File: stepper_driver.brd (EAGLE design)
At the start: 100 x 80 mm, 12 parts, among them IC1 L293D, IC2 L293D, Q1 IRLML5203, Q2 IRLML5203

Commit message: First draft artwork done
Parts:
- added U$6, U$7, U$8, U$9: (no value), holes:3,0
- moved JP3 67.5 mm to (3.81, 34.3), turned to 90 degrees
- moved JP4 28.5 mm to (38.1, 26.7)
- moved IC1 19.3 mm to (20.3, 38.1)
- moved IC2 19.3 mm to (20.3, 15.2)
- moved JP1 19.3 mm to (38.1, 38.1)
- moved JP6 19.3 mm to (38.1, 15.2)
- moved JP5 18.5 mm to (3.81, 26.7)
- moved JP2 13.5 mm to (3.81, 19.1)
- moved Q1 11.7 mm to (10.2, 24.1), turned to 0 degrees
- moved R1 9.16 mm to (21.6, 52.1), turned to 0 degrees
- moved Q2 6.84 mm to (10.2, 47.0), turned to 0 degrees
- moved R2 5.68 mm to (21.6, 49.5), turned to 0 degrees
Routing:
- net N$5: track 0.00 -> 63.9 mm, vias 0 -> 2
- net N$7: track 0.00 -> 49.5 mm
- net IC1_EN: track 0.00 -> 45.1 mm, vias 0 -> 2
- net S2: track 0.00 -> 41.1 mm, vias 0 -> 2
- net S1: track 0.00 -> 35.2 mm, vias 0 -> 2
- net 5V: track 0.00 -> 34.6 mm
- net IC2_EN: track 0.00 -> 34.2 mm
- net VCC: track 0.00 -> 31.4 mm
- net N$3: track 15.8 -> 18.6 mm, vias 0 -> 1
- net N$8: track 15.8 -> 18.6 mm, vias 0 -> 1
- net N$9: track 15.8 -> 18.6 mm, vias 0 -> 1
- net N$2: track 15.8 -> 18.6 mm, vias 0 -> 1
- net N$6: track 29.2 -> 27.3 mm, vias 2 -> 1
- net N$11: track 29.2 -> 27.3 mm, vias 2 -> 1
- net N$4: track 29.2 -> 27.3 mm, vias 2 -> 1
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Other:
- board size 100 x 80 mm -> 42.9 x 55.9 mm
- board text added: "2012 Homin Lee"
- board text added: "Dual L293D driver"

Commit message: Polishing artwork
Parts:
- added C1, C2: (no value), rcl:C1206
- added LED1: (no value), led:LED5MM
- added R3, R4, R5: 1k, rcl:0207/10
- R1, R2: value (none) -> 10k
- moved R1 24.3 mm to (24.1, 27.9)
- moved U$7 4.02 mm to (35.6, 53.3)
- moved U$9 3.81 mm to (35.6, 3.81)
- moved Q2 1.80 mm to (11.4, 45.7)
- moved JP1 1.27 mm to (36.8, 38.1)
- moved JP4 1.27 mm to (36.8, 26.7)
- moved JP6 1.27 mm to (36.8, 15.2)
- moved U$8 1.27 mm to (3.81, 53.3)
- moved JP2 1.27 mm to (2.54, 19.1)
- moved JP3 1.27 mm to (2.54, 34.3)
- moved JP5 1.27 mm to (2.54, 26.7)
- moved IC1 1.27 mm to (19.1, 38.1)
- moved IC2 1.27 mm to (19.1, 15.2)
- moved R2 1.27 mm to (21.6, 50.8), turned to 180 degrees
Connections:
- new net N$10: LED1.K, R3.2
- new net N$12: Q1.3, R1.2, R5.2
- new net N$13: Q2.3, R2.2, R4.1
- net 5V: now also C1.1, C2.1, LED1.A
- net GND: now also C1.2, C2.2, R3.1
- net N$5: now also R5.1; no longer Q1.3, R1.2
- net N$7: now also R4.2; no longer Q2.3, R2.2
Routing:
- net N$5: track 63.9 -> 28.6 mm, vias 2 -> 0
- net N$12: track 0.00 -> 24.0 mm, vias 0 -> 2
- net N$7: track 49.5 -> 30.8 mm
- net N$10: track 0.00 -> 11.0 mm
- net 5V: track 34.6 -> 43.8 mm
- net N$13: track 0.00 -> 8.26 mm
- net IC2_EN: track 34.2 -> 37.9 mm, vias 0 -> 2
- net S2: track 41.1 -> 38.8 mm
- net N$6: track 27.3 -> 26.2 mm
- net N$4: track 27.3 -> 26.2 mm
- net N$11: track 27.3 -> 26.2 mm
- net N$1: track 27.3 -> 26.2 mm
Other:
- board size 42.9 x 55.9 mm -> 39 x 57.1 mm

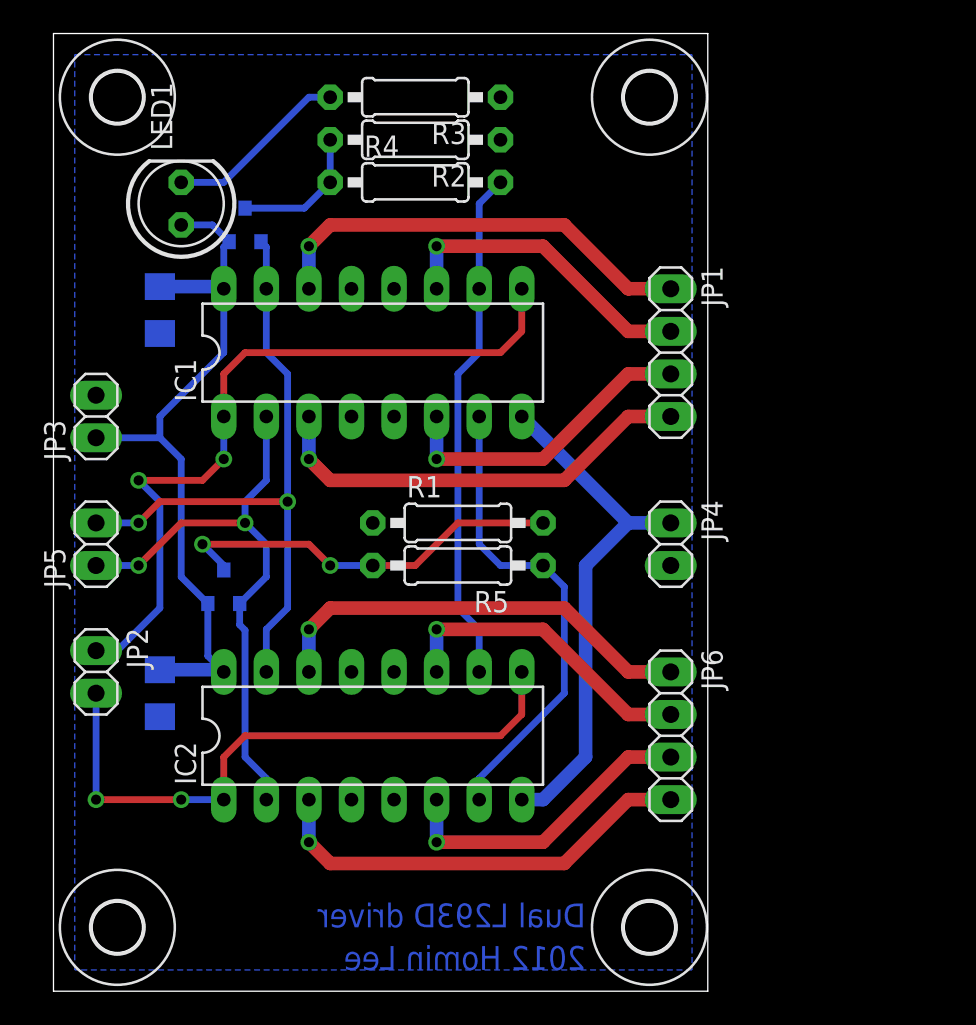
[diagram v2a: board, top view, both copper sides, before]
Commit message: Fix to only for single L293D IC
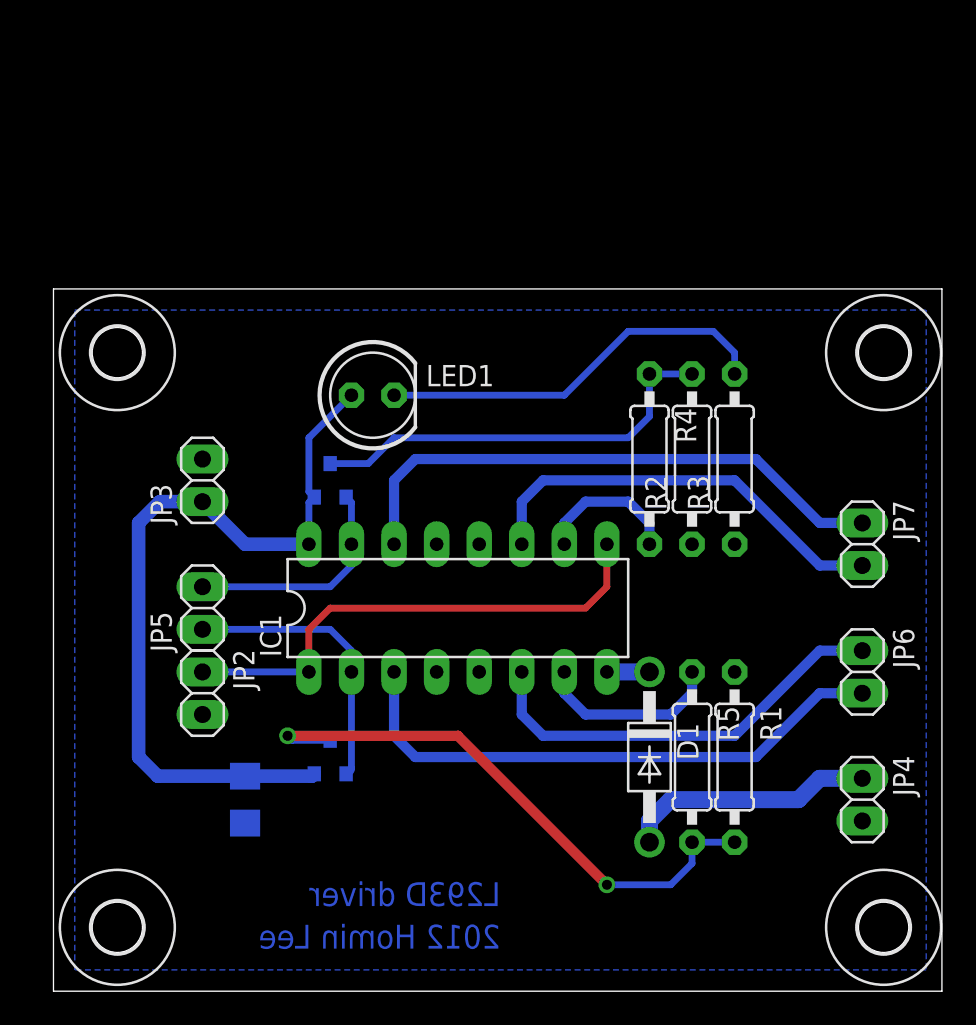
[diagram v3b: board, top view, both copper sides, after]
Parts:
- removed C1: (no value), rcl:C1206
- removed IC2: L293D, st-microelectronics:DIL16
- removed JP1: (no value), pinhead:1X04
- added D1: 1N4004, diode:DO41-10
- added JP7: (no value), pinhead:1X02
- JP6: device pinhead:1X04 -> pinhead:1X02
- moved R3 28.8 mm to (40.6, 31.8), turned to 90 degrees
- moved R2 25.2 mm to (38.1, 31.8), turned to 90 degrees
- moved R1 21.6 mm to (40.6, 14.0), turned to 270 degrees
- moved R4 21.6 mm to (35.6, 31.8), turned to 270 degrees
- moved U$7 20.7 mm to (49.5, 38.1)
- moved JP4 19.1 mm to (48.3, 11.4)
- moved R5 18.1 mm to (38.1, 14.0), turned to 270 degrees
- moved LED1 16.2 mm to (19.1, 35.6), turned to 0 degrees
- moved IC1 16.1 mm to (24.1, 22.9)
- moved Q2 16.1 mm to (16.5, 30.5)
- moved U$8 15.2 mm to (3.81, 38.1)
- moved U$9 14.0 mm to (49.5, 3.81)
- moved JP6 12.0 mm to (48.3, 19.1)
- moved Q1 12.0 mm to (16.5, 14.0)
- moved C2 8.13 mm to (11.4, 11.4)
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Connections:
- removed net N$11: IC2.14, JP6.1
- removed net N$8: IC2.6, JP6.3
- removed net N$9: IC2.11, JP6.2
- net 5V: no longer C1.1, IC2.16
- net GND: no longer C1.2, IC2.12, IC2.13, IC2.4, IC2.5
- net IC2_EN: no longer IC2.1, IC2.9
- net N$1: now also JP6.2; no longer JP1.4
- net N$2: now also JP6.1; no longer JP1.3
- net N$3: now also JP7.2; no longer JP1.2
- net N$4: now also JP7.1; no longer JP1.1
- net N$5: no longer IC2.7
- net N$6: now also D1.C, IC1.8; no longer IC2.3, JP6.4
- net N$7: no longer IC2.10
- net S1: no longer IC2.2
- net S2: no longer IC2.15
- net VCC: now also D1.A; no longer IC1.8, IC2.8
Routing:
- net IC2_EN: track 37.9 -> 0.00 mm, vias 2 -> 0
- net N$11: track 26.2 -> 0.00 mm, vias 1 -> 0
- net S2: track 38.8 -> 13.6 mm, vias 2 -> 0
- net N$6: track 26.2 -> 2.54 mm, vias 1 -> 0
- net N$7: track 30.8 -> 8.67 mm
- net N$8: track 18.6 -> 0.00 mm, vias 1 -> 0
- net N$9: track 18.6 -> 0.00 mm, vias 1 -> 0
- net S1: track 35.2 -> 16.9 mm, vias 2 -> 0
- net N$5: track 28.6 -> 11.2 mm
- net N$13: track 8.26 -> 25.3 mm
- net VCC: track 31.4 -> 15.0 mm
- net IC1_EN: track 45.1 -> 30.3 mm, vias 2 -> 0
- net N$10: track 11.0 -> 23.7 mm
- net N$12: track 24.0 -> 34.8 mm
- net N$1: track 26.2 -> 33.9 mm, vias 1 -> 0
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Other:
- board size 39 x 57.1 mm -> 53 x 41.9 mm
- board text added: "L293D driver"
- board text removed: "Dual L293D driver"
